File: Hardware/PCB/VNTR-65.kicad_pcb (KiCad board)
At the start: 4 copper layers, 370 x 120 mm, 131 parts, among them J1 USB_C_Receptacle, J4 SM03B-SRSS-TB, SW1 SW_Push, SW2 SW_Push, SW3 RotaryEncoder, U1 RP2350_80QFN, U10 SW_MX_HE, U11 SW_MX_HE, U12 SW_MX_HE, U13 SW_MX_HE, U14 SW_MX_HE, U15 SW_MX_HE, U16 SW_MX_HE, U17 SW_MX_HE, U18 SW_MX_HE, U19 SW_MX_HE, U2 NCP1117-3.3_SOT223, U20 SW_MX_HE, U21 SW_MX_HE, U22 SW_MX_HE, U23 SW_MX_HE, U24 SW_MX_HE, U25 SW_MX_HE, U26 SW_MX_HE, U27 SW_MX_HE, U28 SW_MX_HE, U29 SW_MX_HE, U30 SW_MX_HE, U31 SW_MX_HE, U32 SW_MX_HE, U33 SW_MX_HE, U34 SW_MX_HE, U35 SW_MX_HE, U36 SW_MX_HE, U37 SW_MX_HE, U38 SW_MX_HE, U39 SW_MX_HE, U4 CH221K, U40 SW_MX_HE, U41 SW_MX_HE, U42 SW_MX_HE, U43 SW_MX_HE, U44 SW_MX_HE, U45 SW_MX_HE, U46 SW_MX_HE, U47 SW_MX_HE, U48 SW_MX_HE, U49 SW_MX_HE, U5 CD74HC4067M, U50 SW_MX_HE, U51 SW_MX_HE, U52 SW_MX_HE, U53 SW_MX_HE, U54 SW_MX_HE, U55 SW_MX_HE, U56 SW_MX_HE, U57 SW_MX_HE, U58 SW_MX_HE, U59 SW_MX_HE, U6 CD74HC4067M, U60 SW_MX_HE, U61 SW_MX_HE, U62 SW_MX_HE, U63 SW_MX_HE, U64 SW_MX_HE, U65 SW_MX_HE, U66 SW_MX_HE, U67 SW_MX_HE, U68 SW_MX_HE, U69 SW_MX_HE, U7 CD74HC4067M, U70 SW_MX_HE, U71 SW_MX_HE, U72 SW_MX_HE, U73 SW_MX_HE, U74 SW_MX_HE, U75 SW_MX_HE, U76 SW_MX_HE, U77 SW_MX_HE, U78 ER_OLEDM0.91_1x-I2C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

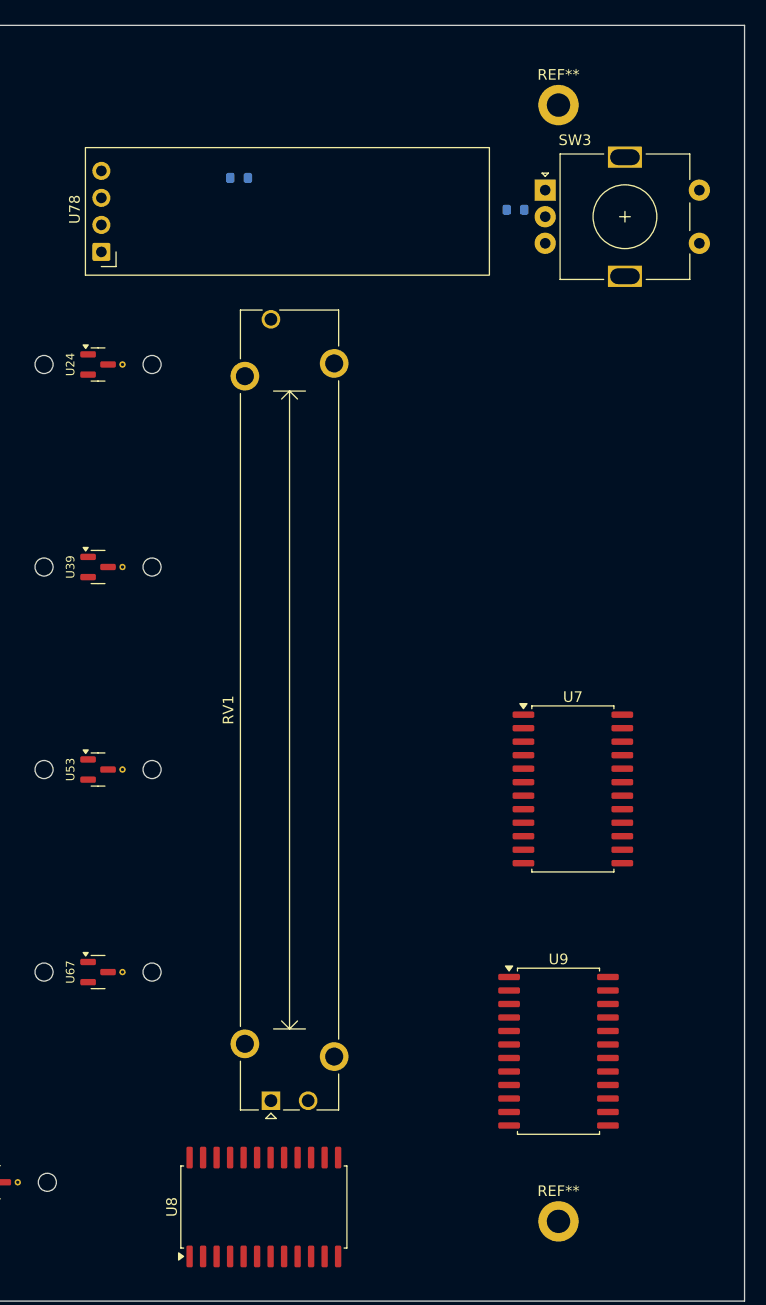
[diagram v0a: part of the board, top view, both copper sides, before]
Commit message: Reorganised the whole 3d models folder and also redid the case sizing
I redid the case sizing so that now it fits the desired size and will
feel more comfortable to use, I made the wood part of the case in
onshape and added it in to the blender file, I redid the sizing of the
pcb so that it looks right, I added in the ec11 encoder the .91' screen
and a knob for the sliding pot as I couldnt get the actual sliding pot
schematic.
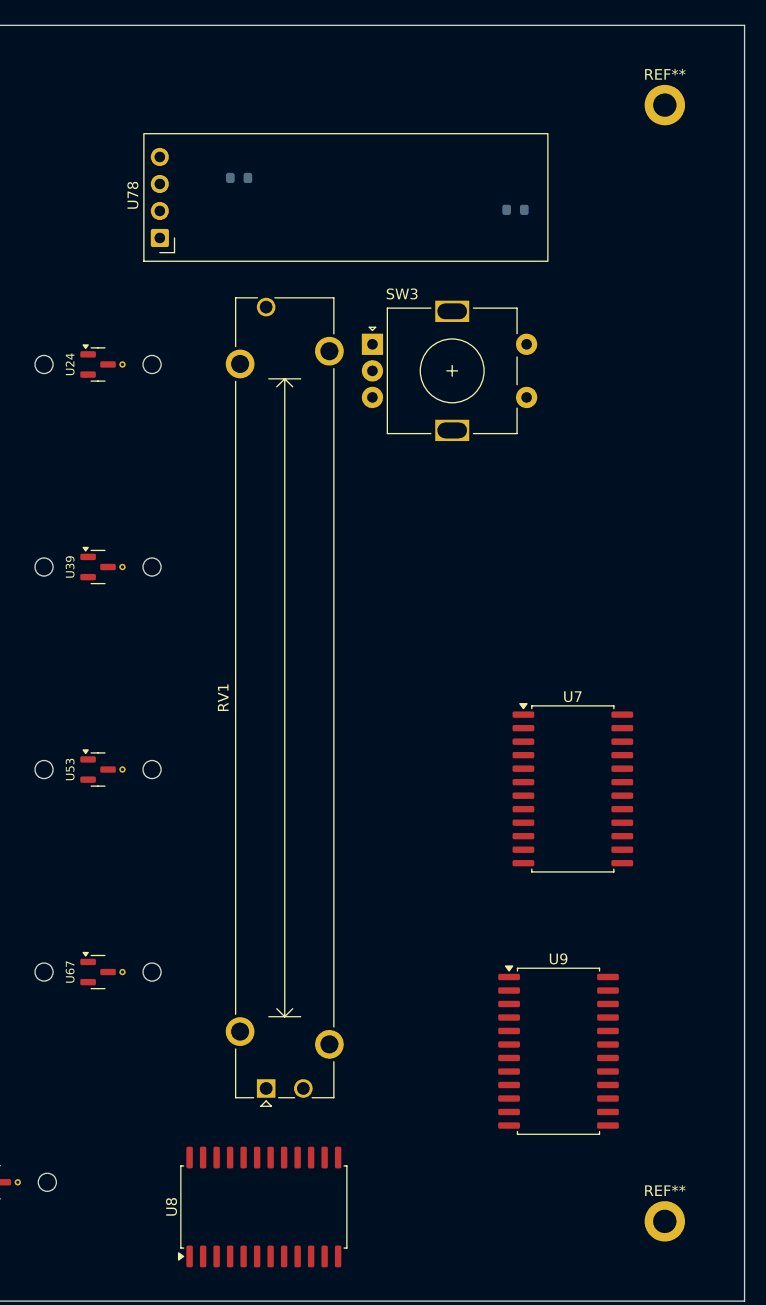
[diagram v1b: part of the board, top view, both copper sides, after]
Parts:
- moved SW3 21.8 mm to (335.0, 30.0)
- moved REF** 10.0 mm to (362.5, 7.50)
- moved REF** 10.0 mm to (362.5, 112.5)
- moved U78 5.65 mm to (315.0, 20.0)
- moved RV1 1.23 mm to (325.0, 100.0)
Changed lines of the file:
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@@
 	(footprint "PCM_Potentiometer_THT_AKL:Potentiometer_Bourns_PTA6043_Single_Slide"
 		(layer "F.Cu")
-		(at 325.45 101.15 90)
+		(at 325 100 90)
 		(descr "Bourns single-gang slide potentiometer, 60.0mm travel, https://www.bourns.com/docs/Product-Datasheets/pta.pdf")
 		(tags "Bourns single-gang slide potentiometer 60.0mm")
@@
 	(footprint "MountingHole:MountingHole_2.2mm_M2_DIN965_Pad"
 		(layer "F.Cu")
-		(at 352.5 7.5)
+		(at 362.5 7.5)
 		(descr "Mounting Hole 2.2mm, M2, generated by kicad-footprint-generator mountinghole.py")
 		(tags "mountinghole M2 DIN965")
@@
 	(footprint "Display:ER_OLEDM0.91_1x-I2C"
 		(layer "F.Cu")
-		(at 309.5 21.31 90)
+		(at 315 20 90)
 		(descr "SSD1306 OLED module, 0.91 inch, 128x32, I2C (https://www.buydisplay.com/download/manual/ER-OLEDM0.91-1_Datasheet.pdf)")
 		(tags "EastRising")
@@
 		)
 		(fp_text user "${REFERENCE}"
-			(at 3.81 17.5 0)
+			(at 5 15 0)
 			(unlocked yes)
 			(layer "F.Fab")
@@
 	(footprint "Rotary_Encoder:RotaryEncoder_Alps_EC11E-Switch_Vertical_H20mm"
 		(layer "F.Cu")
-		(at 351.25 15.5)
+		(at 335 30)
 		(descr "Alps rotary encoder, EC11E... with switch, vertical shaft, http://www.alps.com/prod/info/E/HTML/Encoder/Incremental/EC11/EC11E15204A3.html")
 		(tags "rotary encoder")
@@
 		)
 		(property "Value" "RotaryEncoder"
-			(at 7.5 10.4 0)
+			(at 7.5 10 0)
 			(layer "F.Fab")
 			(effects
@@
 	(footprint "MountingHole:MountingHole_2.2mm_M2_DIN965_Pad"
 		(layer "F.Cu")
-		(at 352.5 112.5)
+		(at 362.5 112.5)
 		(descr "Mounting Hole 2.2mm, M2, generated by kicad-footprint-generator mountinghole.py")
 		(tags "mountinghole M2 DIN965")

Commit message: Reroute the whole pcb so that it works for the new sizing and added in stabilizers
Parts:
- added REF**: STAB_MX_6.25u, PCM_marbastlib-mx:STAB_MX_6.25u, F.Cu at (135.5, 108.0)
- added REF**: STAB_MX_2u, PCM_marbastlib-mx:STAB_MX_2u, F.Cu at (268.4, 69.0)
- added REF**: STAB_MX_2u, PCM_marbastlib-mx:STAB_MX_2u, F.Cu at (271.0, 31.0)
- added REF**: STAB_MX_2u, PCM_marbastlib-mx:STAB_MX_2u, F.Cu at (25.5, 89.0)
- moved C18 3.11 mm to (153.5, 23.5)
- moved C24 0.77 mm to (158.0, 21.3)
- moved R3 0.51 mm to (166.0, 15.2)
- moved Y1 0.16 mm to (155.0, 18.5)
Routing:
- net GND: track 0.00 -> 486.0 mm, vias 0 -> 47
- net GPIO3: track 0.00 -> 377.7 mm, vias 0 -> 12
- net Net-(U54-VOUT): track 0.00 -> 376.3 mm, vias 0 -> 8
- net GPIO4: track 0.00 -> 367.9 mm, vias 0 -> 26
- net GPIO1: track 0.00 -> 366.7 mm, vias 0 -> 20
- net GPIO2: track 0.00 -> 363.6 mm, vias 0 -> 24
- net Net-(U26-VOUT): track 0.00 -> 332.7 mm, vias 0 -> 8
- net Net-(U68-VOUT): track 0.00 -> 322.4 mm, vias 0 -> 4
- net Net-(U55-VOUT): track 0.00 -> 321.3 mm, vias 0 -> 4
- net Net-(U27-VOUT): track 0.00 -> 310.2 mm, vias 0 -> 8
- net Net-(U69-VOUT): track 0.00 -> 301.2 mm, vias 0 -> 4
- net Net-(U56-VOUT): track 0.00 -> 298.6 mm, vias 0 -> 4
- net Net-(U28-VOUT): track 0.00 -> 290.4 mm, vias 0 -> 6
- net Net-(U70-VOUT): track 0.00 -> 276.6 mm, vias 0 -> 4
- net Net-(U57-VOUT): track 0.00 -> 275.2 mm, vias 0 -> 2
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- added copper zone on In1.Cu, net +3V3

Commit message: Updated pcb so that the usb c port isnt 5mm of being centered
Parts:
- moved J1 4.51 mm to (185.0, 5.00)
- moved R9 0.51 mm to (191.0, 11.2)
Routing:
- net /GPIO16: track 171.0 -> 197.0 mm, vias 2 -> 8
- net VBUS: track 36.6 -> 49.5 mm
- net GPIO1: track 366.7 -> 378.6 mm, vias 20 -> 24
- net /USB_D-: track 11.7 -> 17.6 mm, vias 0 -> 4
- net Net-(J1-CC1): track 16.8 -> 11.1 mm, vias 2 -> 0
- net Net-(J1-CC2): track 15.6 -> 20.9 mm
- net ADC3: track 221.9 -> 219.1 mm, vias 21 -> 20
- net /USB_D+: track 18.5 -> 16.6 mm
- net ADC4: track 227.9 -> 226.5 mm
- net /FLASH_SS: track 4.89 -> 5.40 mm
- net GND: vias 47 -> 49
